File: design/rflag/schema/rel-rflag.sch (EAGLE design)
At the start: 4 parts, among them IC1 74LS02N, IC2 74LS08N, IC3 74LS173N, IC4 74LS173N

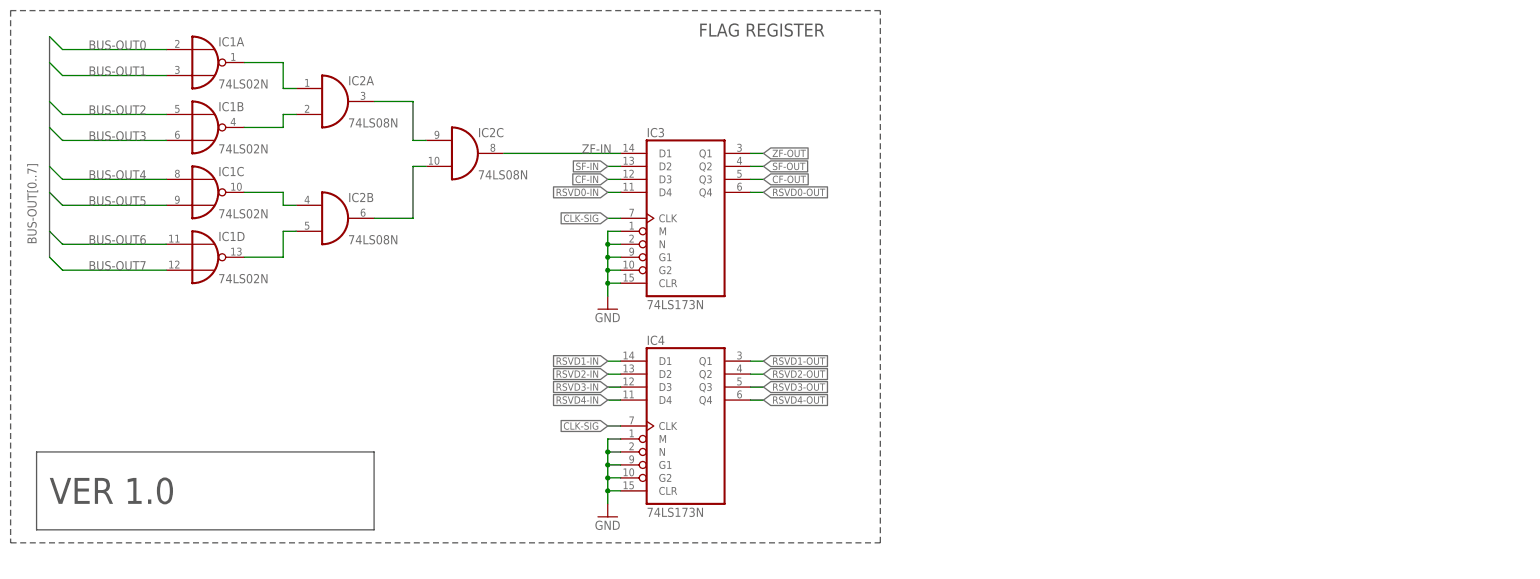
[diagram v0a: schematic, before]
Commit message: Added LEDs and buffer for flag register
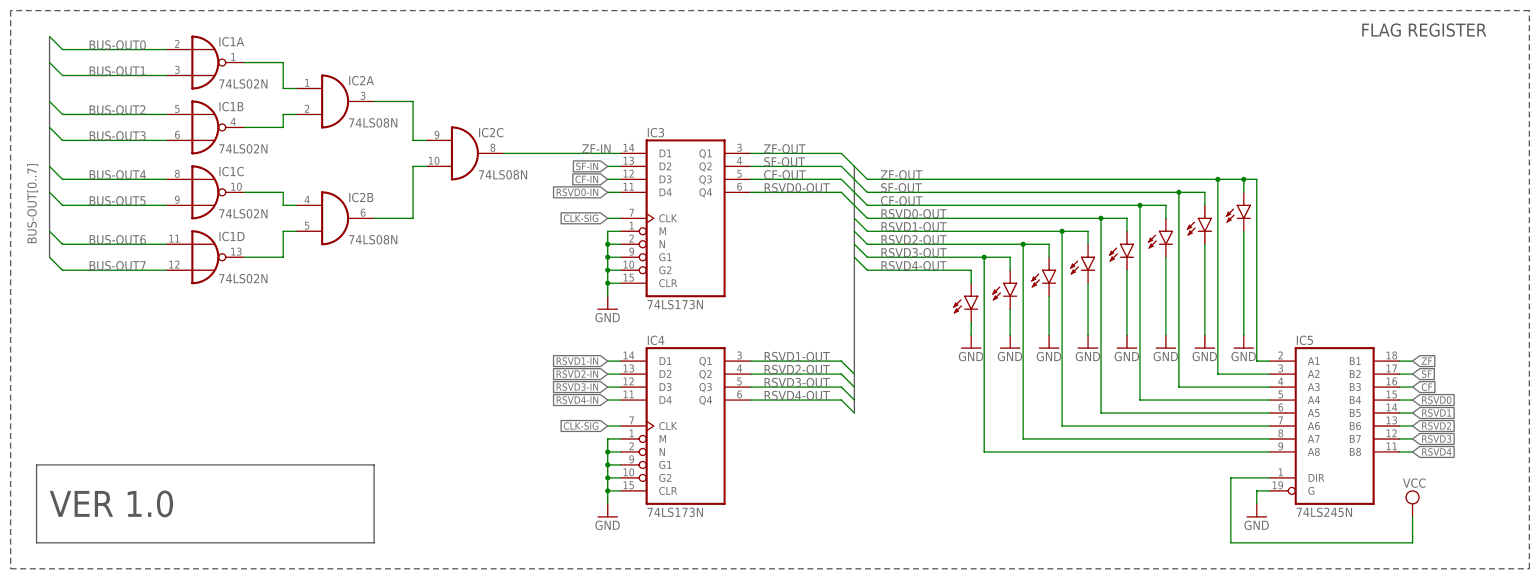
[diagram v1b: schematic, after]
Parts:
- added IC5: 74LS245N, 74xx-eu:74LS245N
- added LED1, LED2, LED3, LED4, LED5, LED6, LED7, LED8: (no value), led:LED5MM
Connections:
- new net CF: IC5A.B3
- new net RSVD0: IC5A.B4
- new net RSVD1: IC5A.B5
- new net RSVD2: IC5A.B6
- new net RSVD3: IC5A.B7
- new net RSVD4: IC5A.B8
- new net SF: IC5A.B2
- new net VCC: IC5A.DIR
- new net ZF: IC5A.B1
- net CF-OUT: now also IC5A.A4, LED3.A
- net GND: now also IC5A.G, LED1.C, LED2.C, LED3.C, LED4.C, LED5.C, LED6.C, LED7.C, LED8.C
- net RSVD0-OUT: now also IC5A.A5, LED4.A
- net RSVD1-OUT: now also IC5A.A6, LED5.A
- net RSVD2-OUT: now also IC5A.A7, LED6.A
- net RSVD3-OUT: now also IC5A.A8, LED7.A
- net RSVD4-OUT: now also LED8.A
- net SF-OUT: now also IC5A.A3, LED2.A
- net ZF-OUT: now also IC5A.A1, IC5A.A2, LED1.A
